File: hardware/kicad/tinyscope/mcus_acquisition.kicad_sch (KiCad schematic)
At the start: 26 parts, among them J5 STM32H743, SW1 SW_SPST, U12 STM32H743VITx, X1 25MHz, X2 32k768

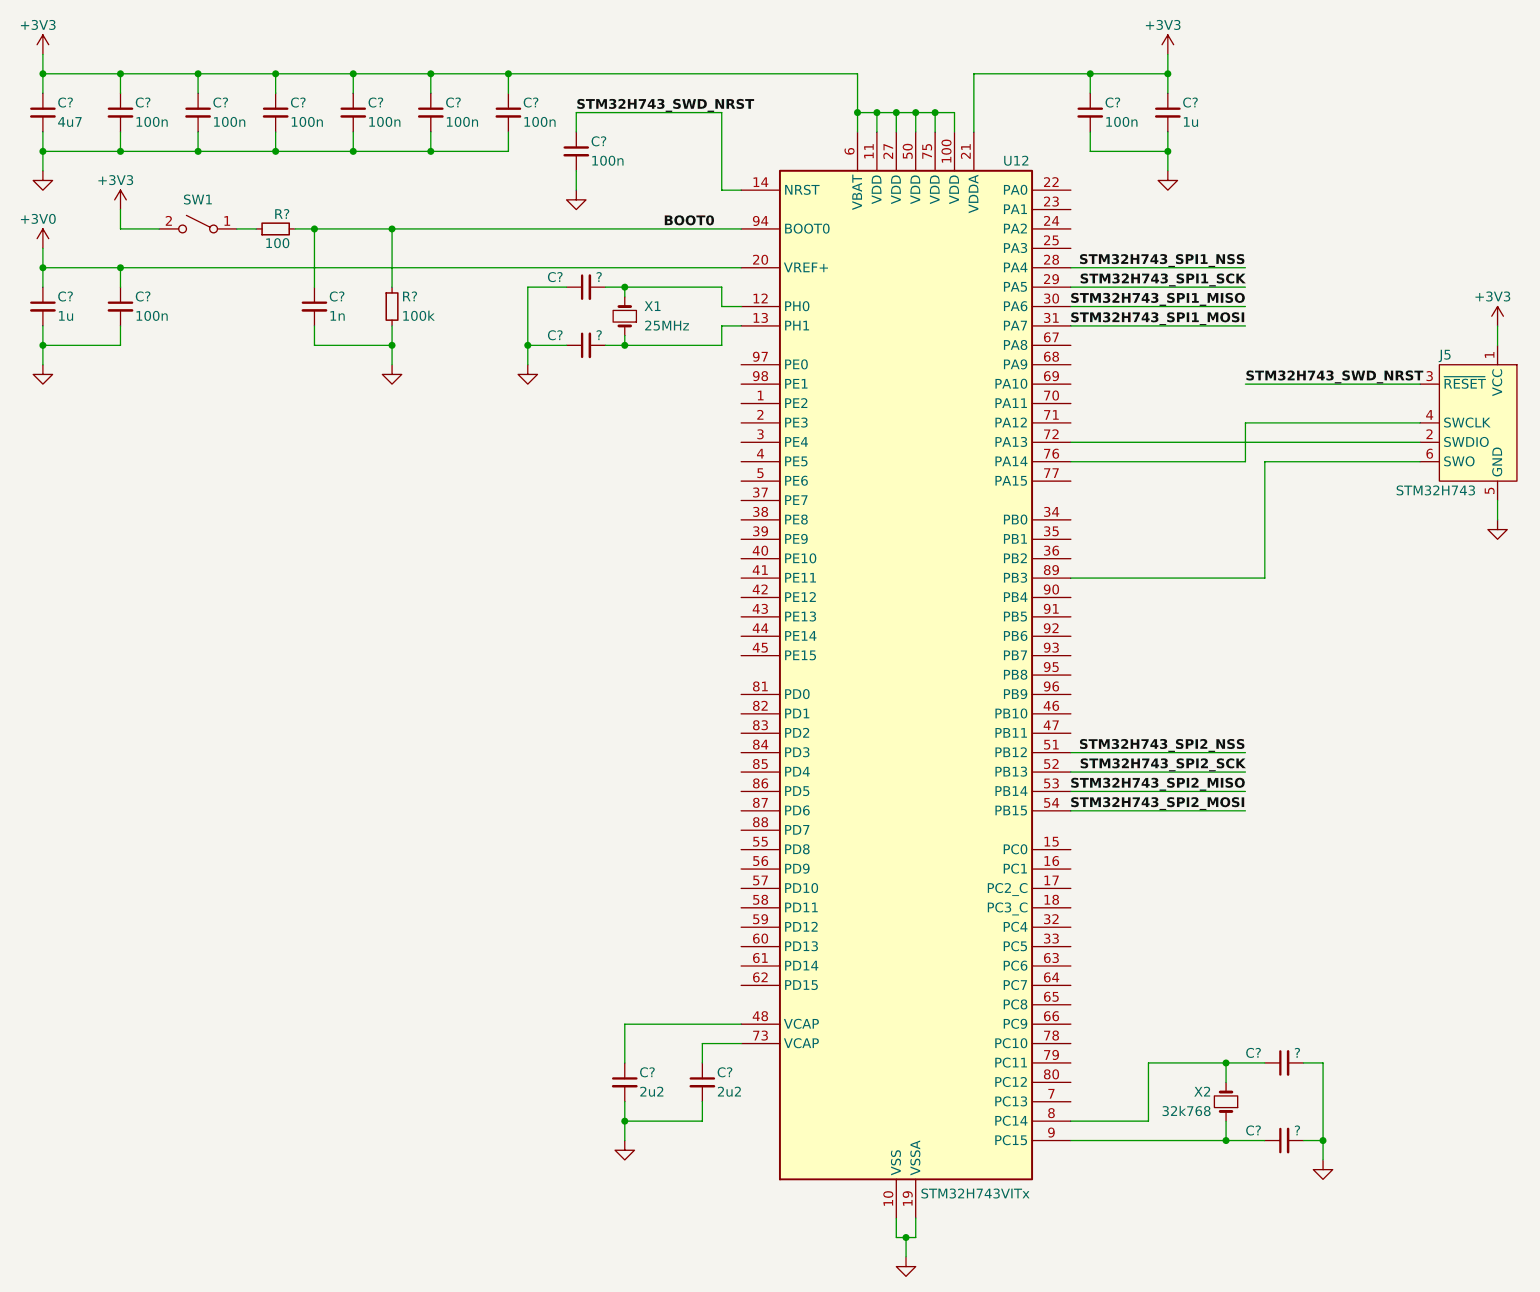
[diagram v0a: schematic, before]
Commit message: feat: hardware: Asigns load capacitors values for STM32H743 and saves crystals datasheet
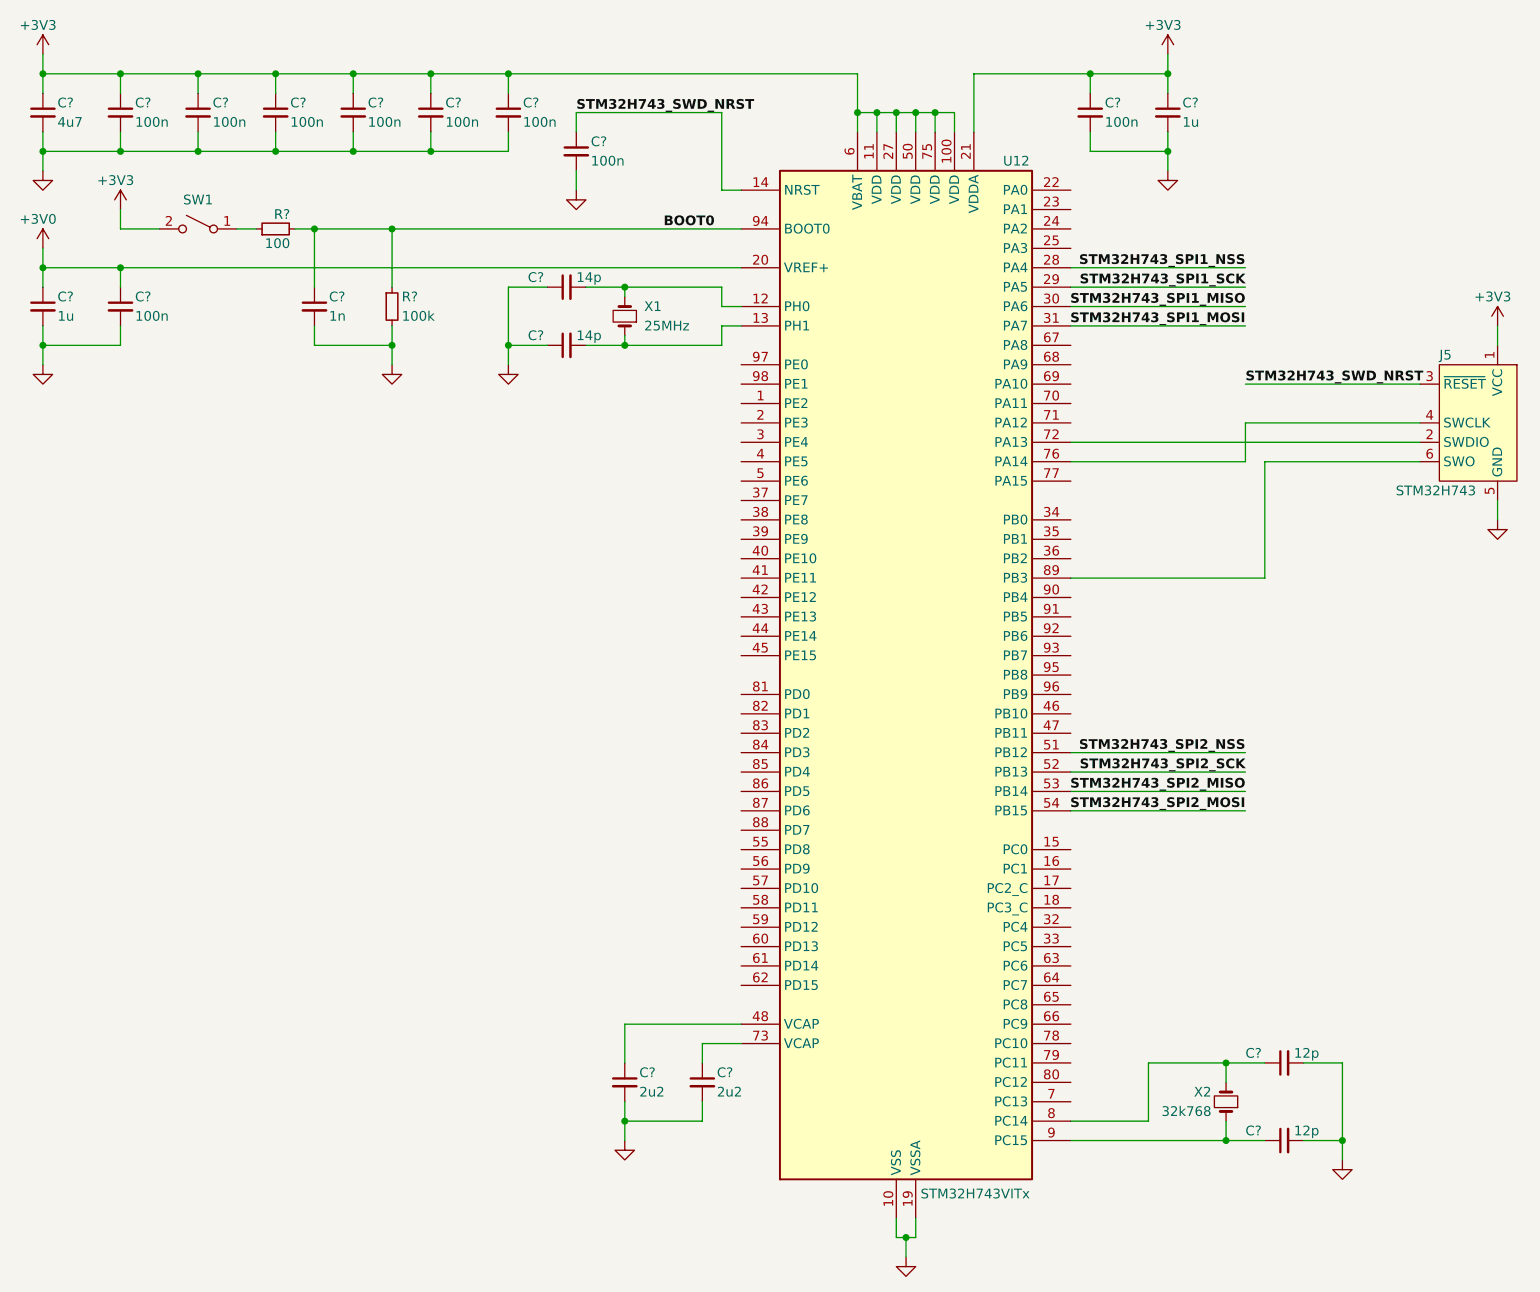
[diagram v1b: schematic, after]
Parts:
- C? (x2): value ? -> 14p
- C? (x2): value ? -> 12p
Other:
- moved on the sheet: C?
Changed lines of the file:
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@@
   (junction (at 119.38 55.88) (diameter 0) (color 0 0 0 0)
   )
-  (junction (at 106.68 55.88) (diameter 0) (color 0 0 0 0)
+  (junction (at 104.14 55.88) (diameter 0) (color 0 0 0 0)
   )
   (junction (at 198.12 160.02) (diameter 0) (color 0 0 0 0)
@@
   (junction (at 93.98 30.48) (diameter 0) (color 0 0 0 0)
   )
-  (junction (at 210.82 160.02) (diameter 0) (color 0 0 0 0)
+  (junction (at 213.36 160.02) (diameter 0) (color 0 0 0 0)
   )
   (junction (at 63.5 20.32) (diameter 0) (color 0 0 0 0)
@@
     (stroke (width 0) (type default))
   )
-  (wire (pts (xy 208.28 149.86) (xy 210.82 149.86))
+  (wire (pts (xy 208.28 149.86) (xy 213.36 149.86))
     (stroke (width 0) (type default))
   )
@@
     (stroke (width 0) (type default))
   )
-  (wire (pts (xy 106.68 55.88) (xy 106.68 58.42))
+  (wire (pts (xy 104.14 55.88) (xy 104.14 58.42))
     (stroke (width 0) (type default))
   )
@@
     (stroke (width 0) (type default))
   )
-  (wire (pts (xy 210.82 149.86) (xy 210.82 160.02))
+  (wire (pts (xy 213.36 149.86) (xy 213.36 160.02))
     (stroke (width 0) (type default))
   )
@@
     (stroke (width 0) (type default))
   )
-  (wire (pts (xy 210.82 160.02) (xy 210.82 162.56))
+  (wire (pts (xy 213.36 160.02) (xy 213.36 162.56))
     (stroke (width 0) (type default))
   )
@@
     (stroke (width 0) (type default))
   )
-  (wire (pts (xy 106.68 48.26) (xy 106.68 55.88))
+  (wire (pts (xy 104.14 48.26) (xy 104.14 55.88))
     (stroke (width 0) (type default))
   )
@@
     (stroke (width 0) (type default))
   )
-  (wire (pts (xy 116.84 55.88) (xy 119.38 55.88))
-    (stroke (width 0) (type default))
-  )
-  (wire (pts (xy 111.76 48.26) (xy 106.68 48.26))
+  (wire (pts (xy 114.3 55.88) (xy 119.38 55.88))
+    (stroke (width 0) (type default))
+  )
+  (wire (pts (xy 109.22 48.26) (xy 104.14 48.26))
     (stroke (width 0) (type default))
   )
@@
     (stroke (width 0) (type default))
   )
-  (wire (pts (xy 116.84 48.26) (xy 119.38 48.26))
+  (wire (pts (xy 114.3 48.26) (xy 119.38 48.26))
     (stroke (width 0) (type default))
   )
@@
     (stroke (width 0) (type default))
   )
-  (wire (pts (xy 111.76 55.88) (xy 106.68 55.88))
+  (wire (pts (xy 109.22 55.88) (xy 104.14 55.88))
     (stroke (width 0) (type default))
   )
@@
     (stroke (width 0) (type default))
   )
-  (wire (pts (xy 208.28 160.02) (xy 210.82 160.02))
+  (wire (pts (xy 208.28 160.02) (xy 213.36 160.02))
     (stroke (width 0) (type default))
   )
@@
     )
   )
-  (symbol (lib_id "Device:C_Small") (at 114.3 48.26 90) (mirror x) (unit 1)
-    (in_bom yes) (on_board yes) (dnp no)
-    (property "Reference" "C?" (at 109.22 46.99 90)
-      (effects (font (size 1.27 1.27)) (justify right))
-    )
-    (property "Value" "?" (at 115.57 46.99 90)
-      (effects (font (size 1.27 1.27)) (justify right))
-    )
-    (property "Footprint" "" (at 114.3 48.26 0)
-      (effects (font (size 1.27 1.27)) hide)
-    )
-    (property "Datasheet" "~" (at 114.3 48.26 0)
+  (symbol (lib_id "Device:C_Small") (at 111.76 48.26 90) (mirror x) (unit 1)
+    (in_bom yes) (on_board yes) (dnp no)
+    (property "Reference" "C?" (at 106.68 46.99 90)
+      (effects (font (size 1.27 1.27)) (justify right))
+    )
+    (property "Value" "14p" (at 113.03 46.99 90)
+      (effects (font (size 1.27 1.27)) (justify right))
+    )
+    (property "Footprint" "" (at 111.76 48.26 0)
+      (effects (font (size 1.27 1.27)) hide)
+    )
+    (property "Datasheet" "~" (at 111.76 48.26 0)
       (effects (font (size 1.27 1.27)) hide)
     )
@@
       (effects (font (size 1.27 1.27)) hide)
     )
-    (property "Datasheet" "~" (at 198.12 154.94 0)
+    (property "Datasheet" "https://eu.mouser.com/ProductDetail/Micro-Crystal/CM8V-T1A-32.768k-9pF-20PPM-TB-QA?qs=7bTaA%2FLYtSYubImfsRD7KQ%3D%3D" (at 198.12 154.94 0)
       (effects (font (size 1.27 1.27)) hide)
     )
@@
       (effects (font (size 1.27 1.27)) hide)
     )
-    (property "Datasheet" "~" (at 119.38 52.07 0)
+    (property "Datasheet" "https://www.mouser.pl/ProductDetail/Wurth-Elektronik/830059800?qs=2WXlatMagcGbm%252B%2F3iLFXdA%3D%3D" (at 119.38 52.07 0)
       (effects (font (size 1.27 1.27)) hide)
     )
@@
       (effects (font (size 1.27 1.27)) (justify right))
     )
-    (property "Value" "?" (at 207.01 148.59 90)
+    (property "Value" "12p" (at 207.01 148.59 90)
       (effects (font (size 1.27 1.27)) (justify right))
     )
@@
     )
   )
-  (symbol (lib_id "Device:C_Small") (at 114.3 55.88 90) (mirror x) (unit 1)
-    (in_bom yes) (on_board yes) (dnp no)
-    (property "Reference" "C?" (at 109.22 54.61 90)
-      (effects (font (size 1.27 1.27)) (justify right))
-    )
-    (property "Value" "?" (at 115.57 54.61 90)
-      (effects (font (size 1.27 1.27)) (justify right))
-    )
-    (property "Footprint" "" (at 114.3 55.88 0)
-      (effects (font (size 1.27 1.27)) hide)
-    )
-    (property "Datasheet" "~" (at 114.3 55.88 0)
+  (symbol (lib_id "Device:C_Small") (at 111.76 55.88 90) (mirror x) (unit 1)
+    (in_bom yes) (on_board yes) (dnp no)
+    (property "Reference" "C?" (at 106.68 54.61 90)
+      (effects (font (size 1.27 1.27)) (justify right))
+    )
+    (property "Value" "14p" (at 113.03 54.61 90)
+      (effects (font (size 1.27 1.27)) (justify right))
+    )
+    (property "Footprint" "" (at 111.76 55.88 0)
+      (effects (font (size 1.27 1.27)) hide)
+    )
+    (property "Datasheet" "~" (at 111.76 55.88 0)
       (effects (font (size 1.27 1.27)) hide)
     )
@@
     )
   )
-  (symbol (lib_id "power:GND") (at 210.82 162.56 0) (mirror y) (unit 1)
+  (symbol (lib_id "power:GND") (at 213.36 162.56 0) (mirror y) (unit 1)
     (in_bom yes) (on_board yes) (dnp no) (fields_autoplaced)
-    (property "Reference" "#PWR?" (at 210.82 168.91 0)
-      (effects (font (size 1.27 1.27)) hide)
-    )
-    (property "Value" "GND" (at 210.82 167.64 0)
-      (effects (font (size 1.27 1.27)) hide)
-    )
-    (property "Footprint" "" (at 210.82 162.56 0)
-      (effects (font (size 1.27 1.27)) hide)
-    )
-    (property "Datasheet" "" (at 210.82 162.56 0)
+    (property "Reference" "#PWR?" (at 213.36 168.91 0)
+      (effects (font (size 1.27 1.27)) hide)
+    )
+    (property "Value" "GND" (at 213.36 167.64 0)
+      (effects (font (size 1.27 1.27)) hide)
+    )
+    (property "Footprint" "" (at 213.36 162.56 0)
+      (effects (font (size 1.27 1.27)) hide)
+    )
+    (property "Datasheet" "" (at 213.36 162.56 0)
       (effects (font (size 1.27 1.27)) hide)
     )
@@
       (effects (font (size 1.27 1.27)) (justify right))
     )
-    (property "Value" "?" (at 207.01 158.75 90)
+    (property "Value" "12p" (at 207.01 158.75 90)
       (effects (font (size 1.27 1.27)) (justify right))
     )
@@
     )
   )
-  (symbol (lib_id "power:GND") (at 106.68 58.42 0) (mirror y) (unit 1)
+  (symbol (lib_id "power:GND") (at 104.14 58.42 0) (mirror y) (unit 1)
     (in_bom yes) (on_board yes) (dnp no) (fields_autoplaced)
-    (property "Reference" "#PWR?" (at 106.68 64.77 0)
-      (effects (font (size 1.27 1.27)) hide)
-    )
-    (property "Value" "GND" (at 106.68 63.5 0)
-      (effects (font (size 1.27 1.27)) hide)
-    )
-    (property "Footprint" "" (at 106.68 58.42 0)
-      (effects (font (size 1.27 1.27)) hide)
-    )
-    (property "Datasheet" "" (at 106.68 58.42 0)
-      (effects (font (size 1.27 1.27)) hide)
-    )
+    (property "Reference" "#PWR?" (at 104.14 64.77 0)
+      (effects (font (size 1.27 1.27)) hide)
+    )
+    (property "Value" "GND" (at 104.14 63.5 0)
+      (effects (font (size 1.27 1.27)) hide)
+    )
+    (property "Footprint" "" (at 104.14 58.42 0)
+      (effects (font (size 1.27 1.27)) hide)
+    )
+    (property "Datasheet" "" (at 104.14 58.42 0)
+      (effects (font (size 1.27 1.27)) hide)
+    )

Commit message: feat: hardware: Finish MCU wireless schematic
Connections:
- net STM32H743_SPI1_IRQ: now reaches U12.25 (PA3)
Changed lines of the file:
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@@
+    (stroke (width 0) (type default))
+  )
+  (wire (pts (xy 177.8 43.18) (xy 200.66 43.18))
     (stroke (width 0) (type default))
   )
@@
     (effects (font (size 1.27 1.27) bold) (justify right bottom))
   )
+  (label "STM32H743_SPI1_IRQ" (at 200.66 43.18 180) (fields_autoplaced)
+    (effects (font (size 1.27 1.27) bold) (justify right bottom))
+  )

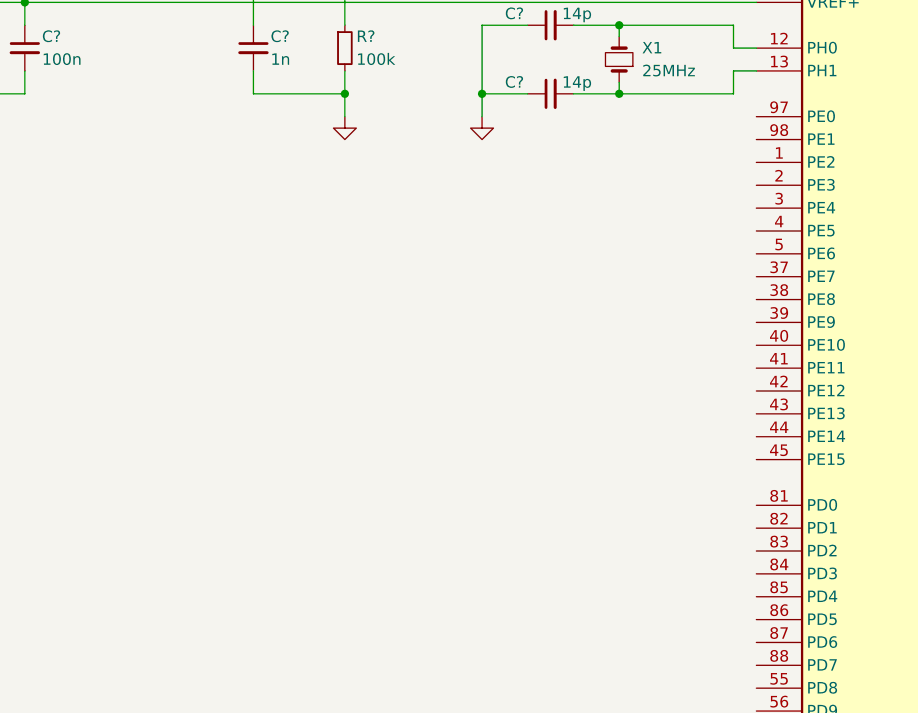
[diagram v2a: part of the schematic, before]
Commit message: feat: hardware: Adds green led mosfet driver for STM32H743
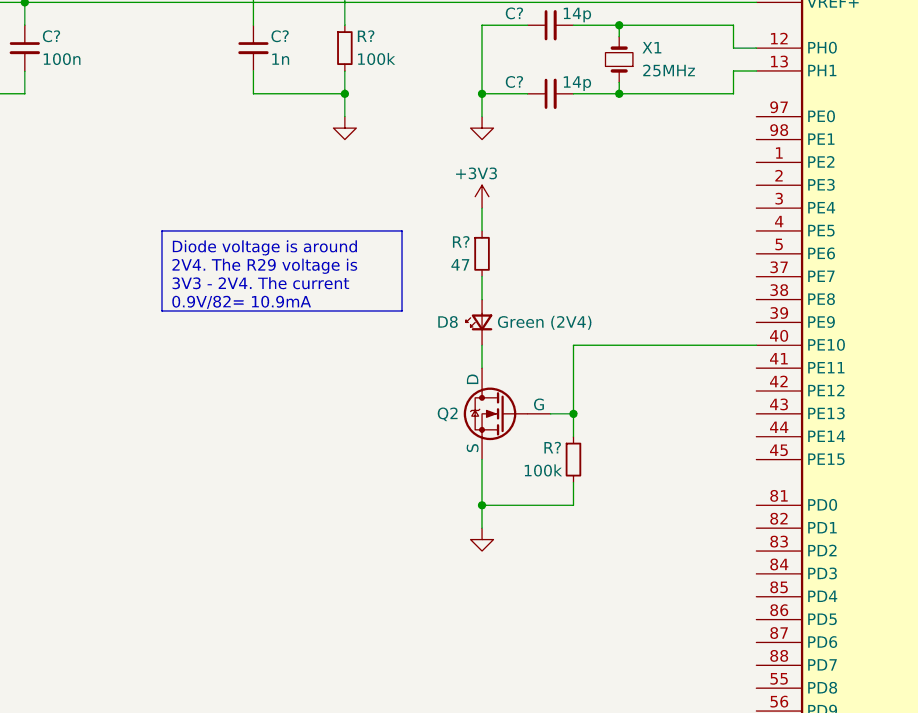
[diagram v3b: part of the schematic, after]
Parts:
- added D8: Green (2V4), symbol Device:LED_Small
- added Q2: NMOS, symbol Simulation_SPICE:NMOS
- added R?: 100k, symbol Device:R_Small
- added R?: 47, symbol Device:R_Small
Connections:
- net +3V3: now also R?.1
- net GND: now also Q2.3 (S), R?.2
- net at U12.40 (PE10): now also Q2.2 (G), R?.1
- new net: D8.1 (K), Q2.1 (D)
- new net: D8.2 (A), R?.2
